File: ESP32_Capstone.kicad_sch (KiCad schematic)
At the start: 60 parts, among them J1 USB_C_Receptacle_USB2.0_16P, J2 B2B-PH-K-S, J3 Conn_01x03, J4 Conn_01x04, J5 Conn_01x02, SW5 SW_Omron_B3FS, SW6 SW_Omron_B3FS, SW7 SW_Omron_B3FS, U1 ESP32-C3, U2 MCP73831T-2ACI_OT, U4 W25Q32JVSS, Y1 40 MHz

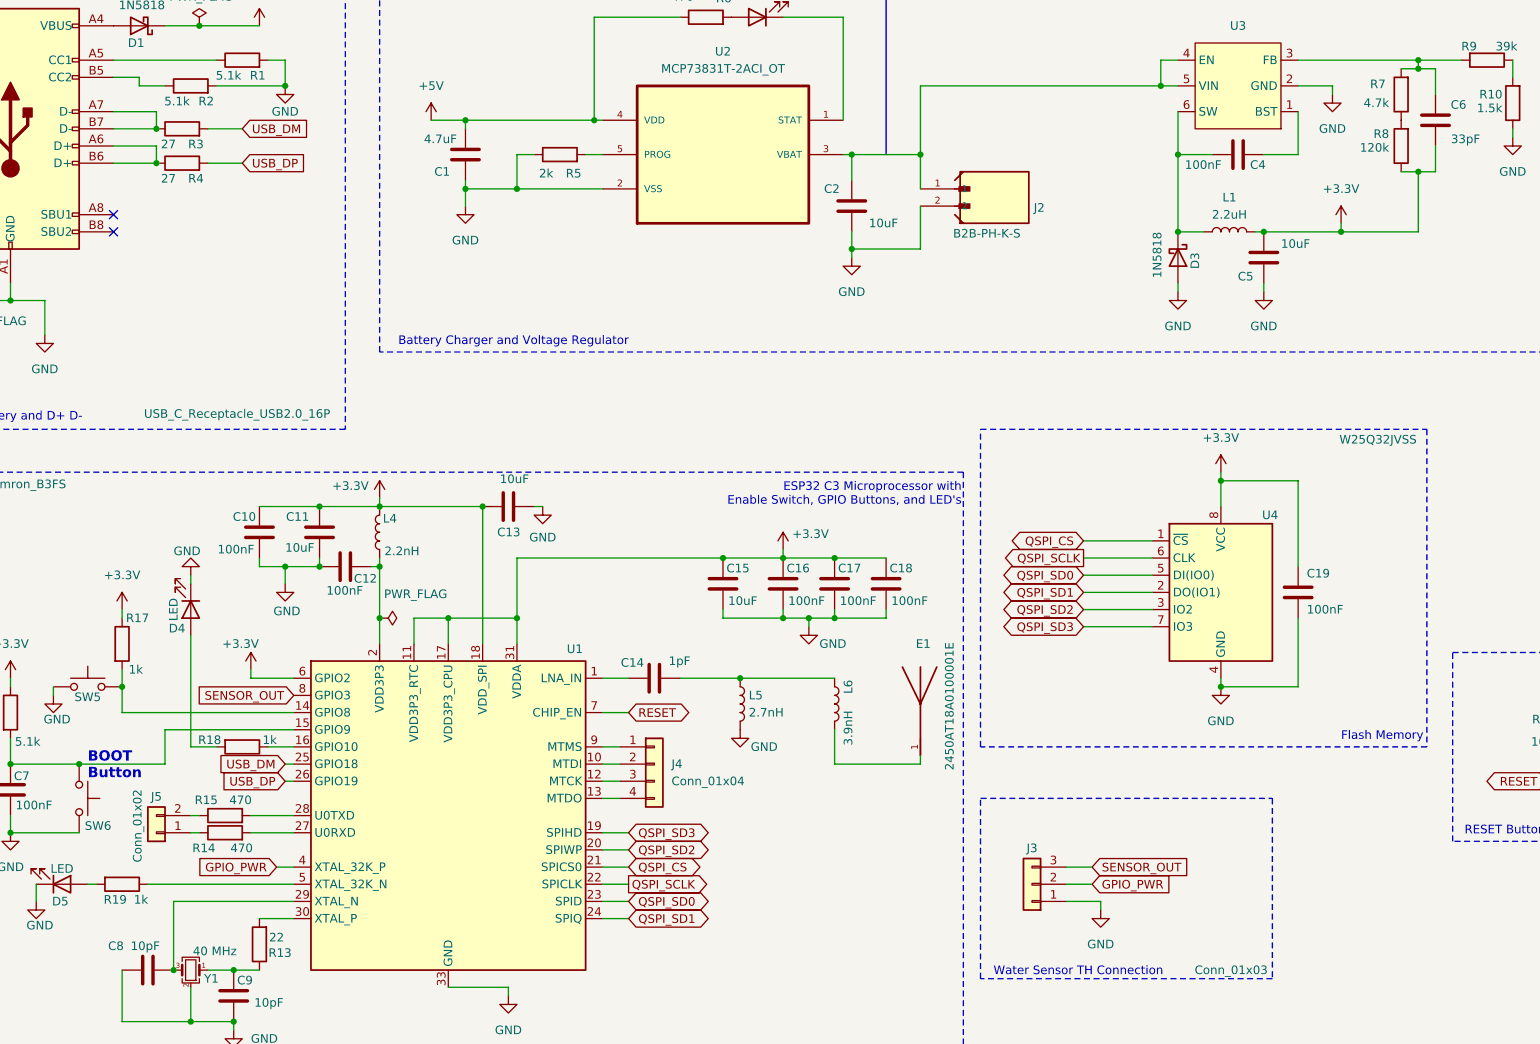
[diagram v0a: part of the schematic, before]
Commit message: Added a Resistor for GPIO 2, pin 6, as recommended to keep pulled-up
All other information is changed as previous commit; List of numbers on the schematic correspond to the notes from McCreight.
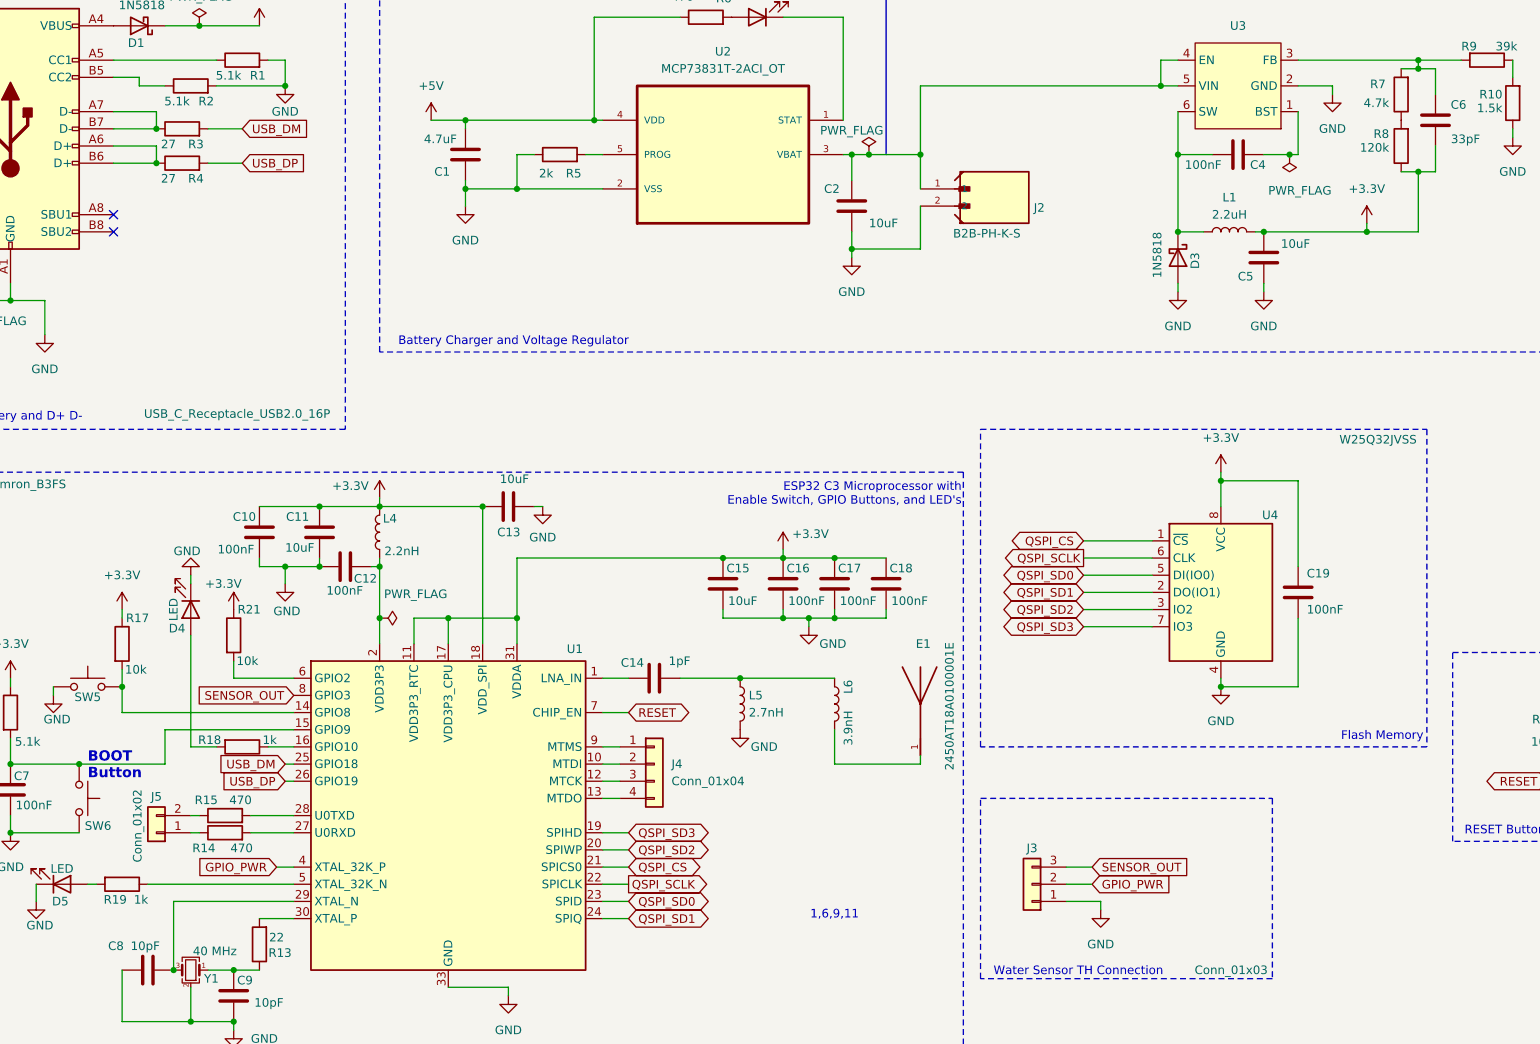
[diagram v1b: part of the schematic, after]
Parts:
- added R21: 10k, Resistor_SMD:R_0805_2012Metric, symbol Device:R
- R17: value 1k -> 10k
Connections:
- net +3.3V: now also R21.1; no longer U1.6 (GPIO2)
- new net: R21.2, U1.6 (GPIO2)
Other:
- note added: "1,6,9,11"
